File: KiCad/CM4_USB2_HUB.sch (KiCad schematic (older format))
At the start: 1 part

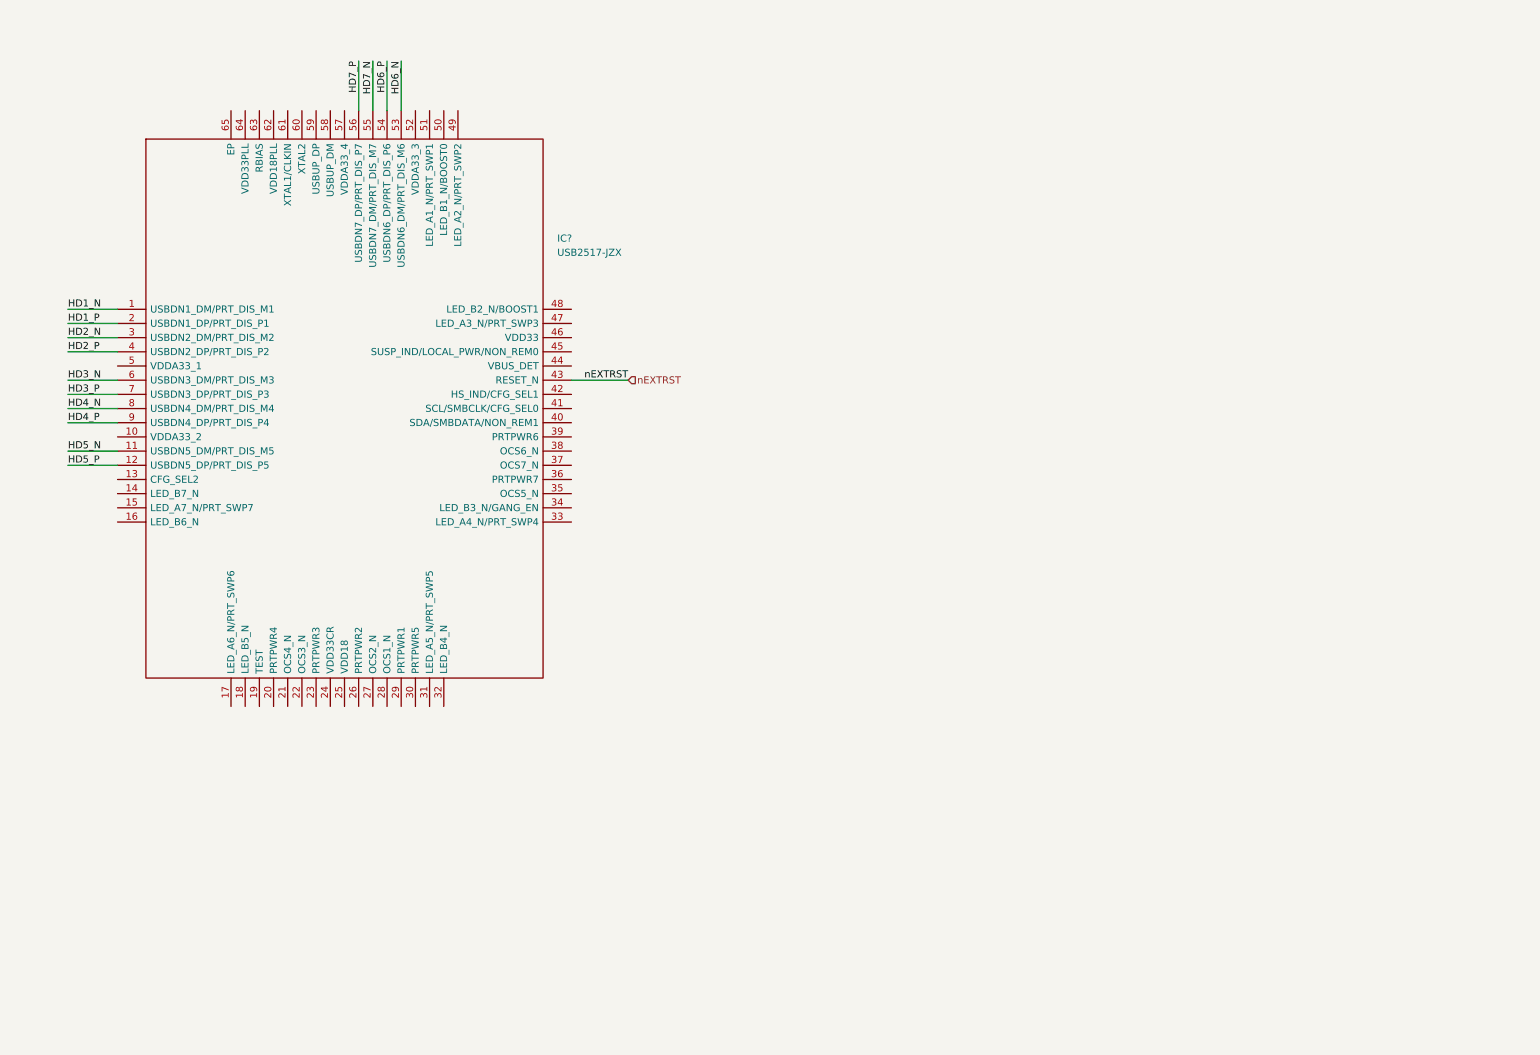
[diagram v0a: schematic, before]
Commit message: Lotsa changes
Added new footprints:
PCIe x1, TO-252 tab, SOT95, SOP50, SON50, Hirose FH-12-22S, 2.54mm 2x02 and 2x05 headers
Added new models:
Hirose FH-12-22S, FSUSB42MUX, MIC2019YM6-TR, TPS6206
Re-did ATX connector symbol wiring
Begun wiring PI7C PCI-e switch
Wired USB2517 hub
Begun adding MIC2019YM6 current limiters.
Added TODO lists to each page to help new contributors
Begun placing PCB footprints and descriptors
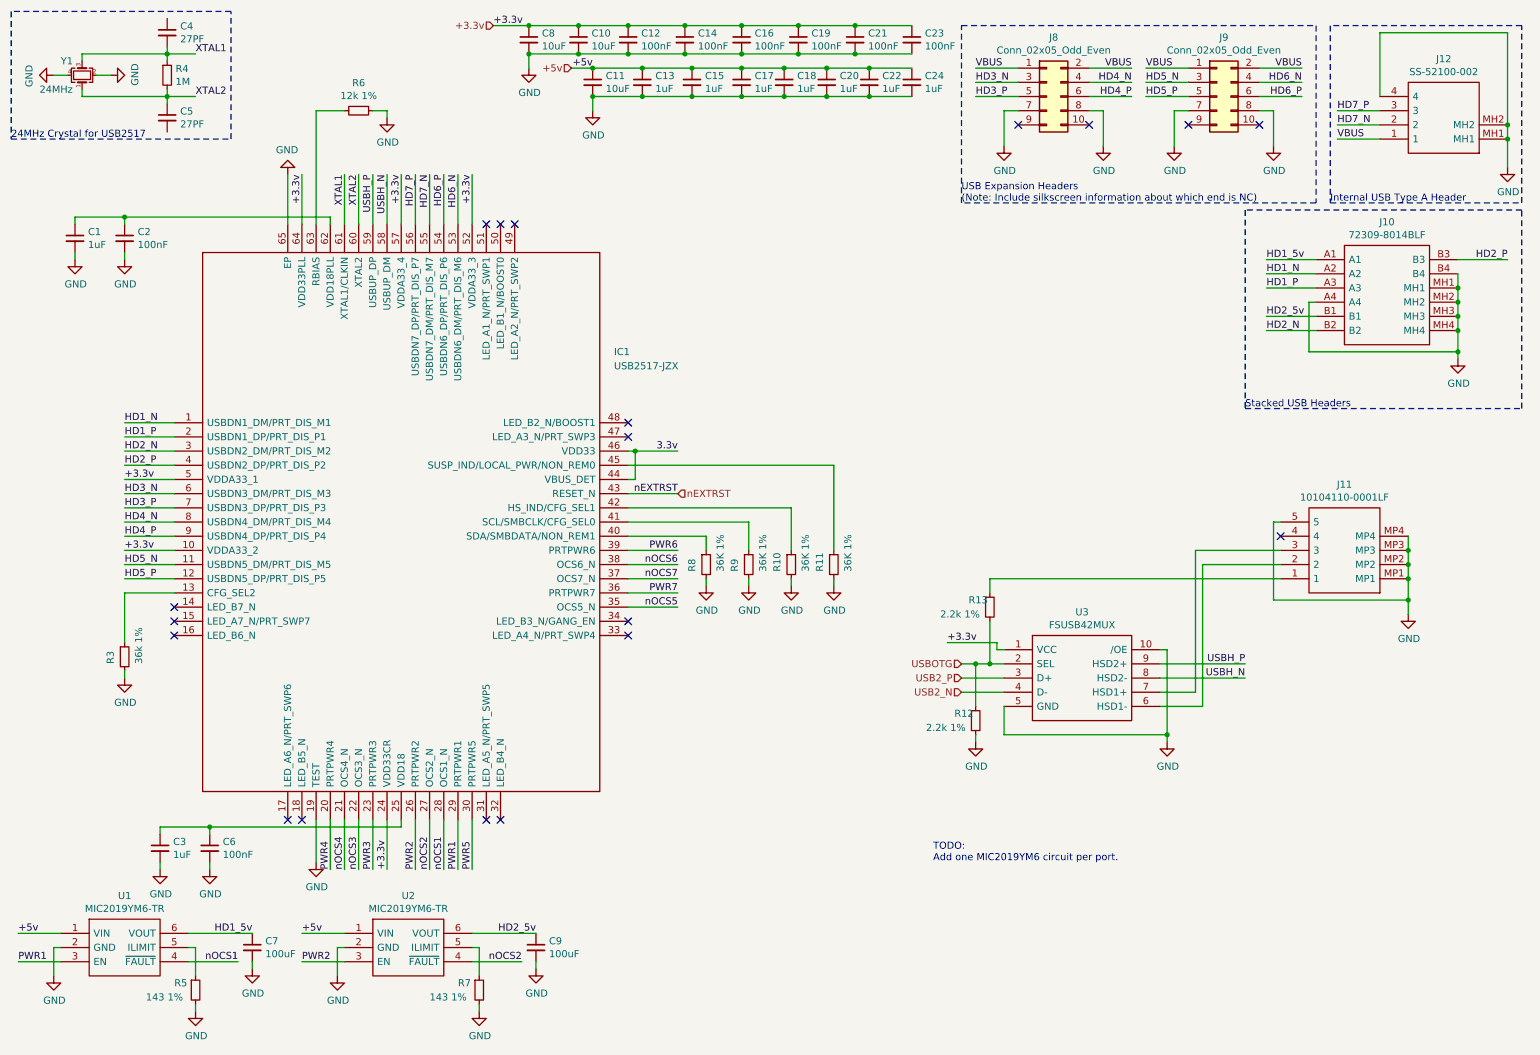
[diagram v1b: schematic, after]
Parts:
- added C1, C13, C15, C17, C18, C20, C22, C24, C3: 1uF, symbol Device:C_Small
- added C10, C11, C8: 10uF, symbol Device:C_Small
- added C12, C14, C16, C19, C2, C21, C23, C6: 100nF, symbol Device:C_Small
- added C4, C5: 27PF, symbol Device:C_Small
- added C7, C9: 100uF, symbol Device:C_Small
- added J10: 72309-8014BLF, 723098014BLF, symbol CM4_MATX:72309-8014BLF
- added J11: 10104110-0001LF, CM4_MATX:101041100001LF, symbol CM4_MATX:10104110-0001LF
- added J12: SS-52100-002, SS52100002, symbol CM4_MATX:SS-52100-002
- added J8, J9: Conn_02x05_Odd_Even, CM4_MATX:PinHeader_2x05_P2.54mm_Vertical, symbol Connector_Generic:Conn_02x05_Odd_Even
- added R10, R11, R8, R9: 36K 1%, symbol Device:R_Small
- added R12, R13: 2.2k 1%, symbol Device:R_Small
- added R3: 36k 1%, symbol Device:R_Small
- added R4: 1M, symbol Device:R_Small
- added R5, R7: 143 1%, symbol Device:R_Small
- added R6: 12k 1%, symbol Device:R_Small
- added U1, U2: MIC2019YM6-TR, SOT95P280X145-6N, symbol CM4_MATX:MIC2019YM6-TR
- added U3: FSUSB42MUX, SOP50P490X110-10N, symbol CM4_MATX:FSUSB42MUX
- added Y1: 24MHz, symbol Device:Crystal_GND24_Small
- gave numbers to parts that had none: 1
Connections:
- net HD1_N: now also J10.A2
- net HD1_P: now also J10.A3
- net HD2_N: now also J10.B2
- net HD2_P: now also J10.B3
- net HD3_N: now also J8.3 (Pin_3)
- net HD3_P: now also J8.5 (Pin_5)
- net HD4_N: now also J8.4 (Pin_4)
- net HD4_P: now also J8.6 (Pin_6)
- net HD5_N: now also J9.3 (Pin_3)
- net HD5_P: now also J9.5 (Pin_5)
- net HD6_N: now also J9.4 (Pin_4)
- net HD6_P: now also J9.6 (Pin_6)
- net HD7_N: now also J12.2
- net HD7_P: now also J12.3
- net +3.3v: now reaches IC1.10 (VDDA33_2)
- net +3.3v: now also IC1.24 (VDD33CR), IC1.5 (VDDA33_1), IC1.52 (VDDA33_3), IC1.57 (VDDA33_4), IC1.64 (VDD33PLL), C10.1, C12.1, C14.1, C16.1, C19.1, C21.1, C23.1, C8.1, U3.1 (VCC)
- net at IC1.13 (CFG_SEL2): now also R3.1
- net GND: now reaches IC1.19 (TEST)
- net GND: now also IC1.65 (EP), C1.2, C10.2, C11.2, C12.2, C13.2, C14.2, C15.2, C16.2, C17.2, C18.2, C19.2, C2.2, C20.2, C21.2, C22.2, C23.2, C24.2, C3.2, C6.2, C7.2, C8.2, C9.2, J10.A4, J10.B4, J10.MH1, J10.MH2, J10.MH3, J10.MH4, J11.5, J11.MP1, J11.MP2, J11.MP3, J11.MP4, J12.4, J12.MH1, J12.MH2, J8.7 (Pin_7), J8.8 (Pin_8), J9.7 (Pin_7), J9.8 (Pin_8), R10.2, R11.2, R12.2, R3.2, R5.2, R6.1, R7.2, R8.2, R9.2, U1.2 (GND), U2.2 (GND), U3.10 (/OE), U3.5 (GND), Y1.2, Y1.4
- net PWR4: now reaches IC1.20 (PRTPWR4)
- net nOCS4: now reaches IC1.21 (OCS4_N)
- net nOCS3: now reaches IC1.22 (OCS3_N)
- net PWR3: now reaches IC1.23 (PRTPWR3)
- net at IC1.25 (VDD18): now also C3.1, C6.1
- net PWR2: now reaches IC1.26 (PRTPWR2)
- net PWR2: now also U2.3 (EN)
- net nOCS2: now reaches IC1.27 (OCS2_N)
- net nOCS2: now also U2.4 (~FAULT)
- net nOCS1: now reaches IC1.28 (OCS1_N)
- net nOCS1: now also U1.4 (~FAULT)
- net PWR1: now reaches IC1.29 (PRTPWR1)
- net PWR1: now also U1.3 (EN)
- net PWR5: now reaches IC1.30 (PRTPWR5)
- net nOCS5: now reaches IC1.35 (OCS5_N)
- net PWR7: now reaches IC1.36 (PRTPWR7)
- net nOCS7: now reaches IC1.37 (OCS7_N)
- net nOCS6: now reaches IC1.38 (OCS6_N)
- net PWR6: now reaches IC1.39 (PRTPWR6)
- net at IC1.40 (SDA/SMBDATA/NON_REM1): now also R8.1
- net at IC1.41 (SCL/SMBCLK/CFG_SEL0): now also R9.1
- net at IC1.42 (HS_IND/CFG_SEL1): now also R10.1
- net 3.3v: now reaches IC1.44 (VBUS_DET)
- net 3.3v: now also IC1.46 (VDD33)
- net at IC1.45 (SUSP_IND/LOCAL_PWR/NON_REM0): now also R11.1
- net USBH_N: now reaches IC1.58 (USBUP_DM)
- net USBH_N: now also U3.8 (HSD2-)
- net USBH_P: now reaches IC1.59 (USBUP_DP)
- net USBH_P: now also U3.9 (HSD2+)
- net XTAL2: now reaches IC1.60 (XTAL2)
- net XTAL2: now also C5.1, R4.2, Y1.1
- net XTAL1: now reaches IC1.61 (XTAL1/CLKIN)
- net XTAL1: now also C4.2, R4.1, Y1.3
- net at IC1.62 (VDD18PLL): now also C1.1, C2.1
- net at IC1.63 (RBIAS): now also R6.2
- new net: J11.2, U3.6 (HSD1-)
- new net: J11.3, U3.7 (HSD1+)
- new net: J11.1, R13.1
- new net: R5.1, U1.5 (ILIMIT)
- new net: R7.1, U2.5 (ILIMIT)
- new net +5v: C11.1, C13.1, C15.1, C17.1, C18.1, C20.1, C22.1, C24.1, U1.1 (VIN), U2.1 (VIN)
- new net HD1_5v: C7.1, J10.A1, U1.6 (VOUT)
- new net HD2_5v: C9.1, J10.B1, U2.6 (VOUT)
- new net USB2_N: U3.4 (D-)
- new net USB2_P: U3.3 (D+)
- new net USBOTG: R12.1, R13.2, U3.2 (SEL)
- new net VBUS: J12.1, J8.1 (Pin_1), J8.2 (Pin_2), J9.1 (Pin_1), J9.2 (Pin_2)
- no-connect marks 0 -> 19
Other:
- note added: "24MHz Crystal for USB2517"
- note added: "Internal USB Type A Header"
- note added: "Stacked USB Headers"
- note added: "TODO:\nAdd one MIC2019YM6 circuit per port."
- note added: "USB Expansion Headers\n(Note: Include silkscreen information about which end is NC)"
- moved on the sheet: IC1

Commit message: Many, many changes...
Added a bunch of new footprints and a couple of new symbols.
Added the other side of the CM4 connector and wired its features.
Added some more detailed models for a fair few components.
Added a new schematic to handle power for USB ports.
Updated the PCB with the new components and moved some around to populate the rear IO panel.
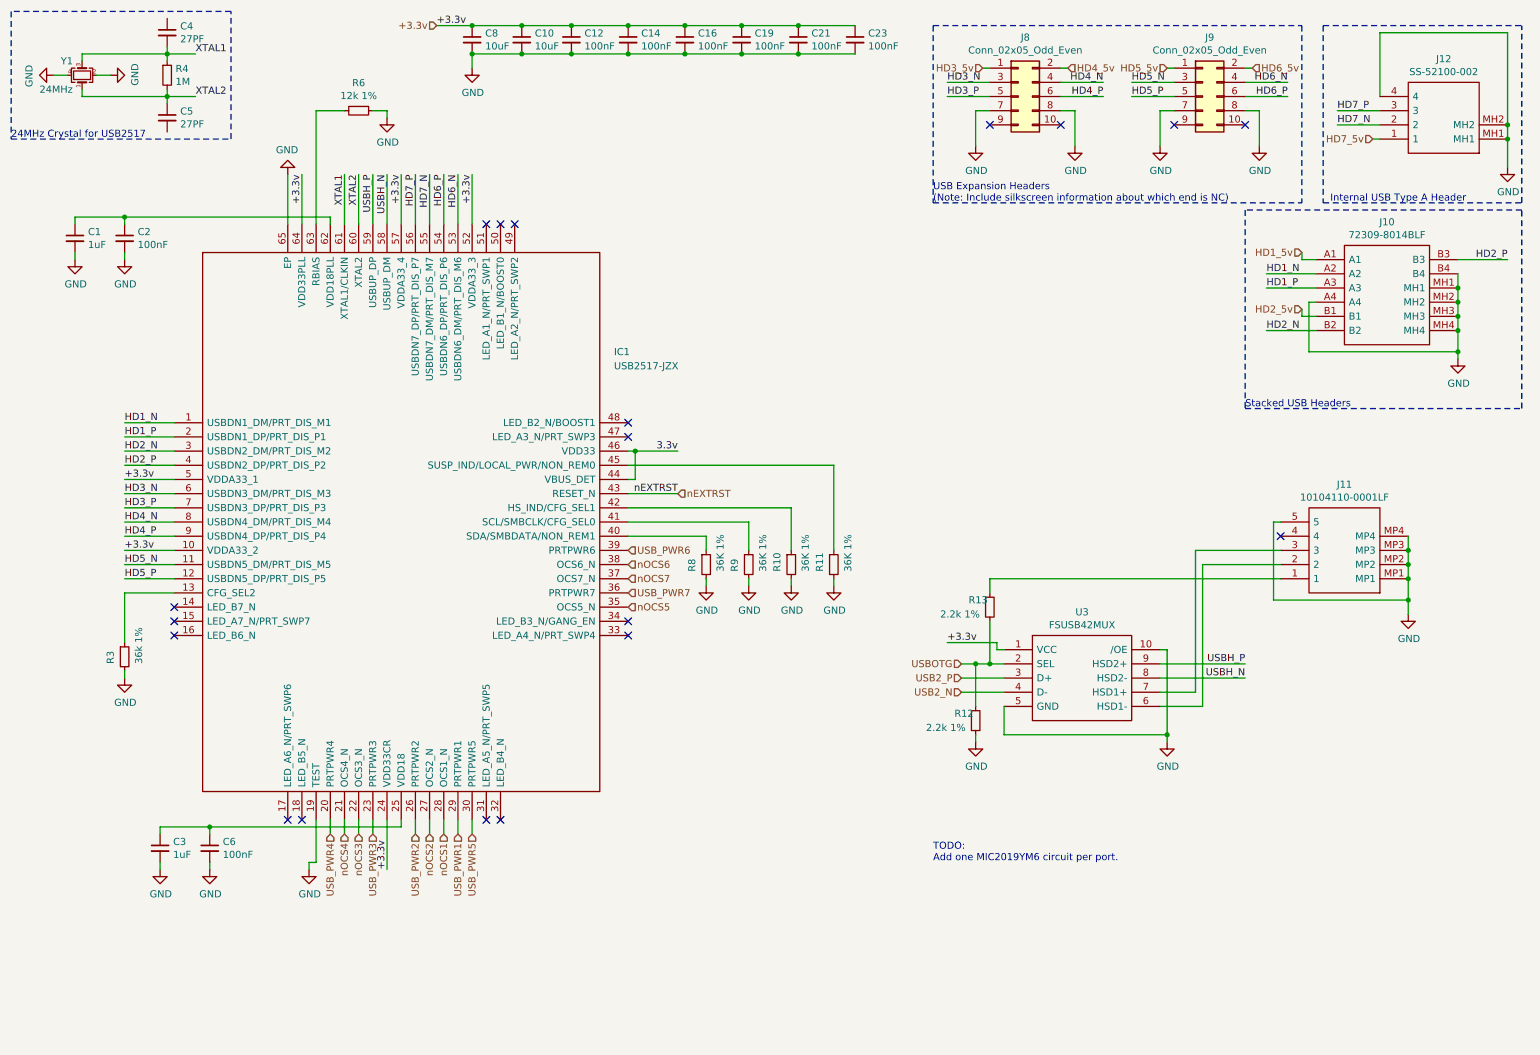
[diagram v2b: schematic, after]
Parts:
- removed C11: 10uF, symbol Device:C_Small
- removed C13, C15, C17, C18, C20, C22, C24: 1uF, symbol Device:C_Small
- removed C7, C9: 100uF, symbol Device:C_Small
- removed R5, R7: 143 1%, symbol Device:R_Small
- removed U1, U2: MIC2019YM6-TR, SOT95P280X145-6N, symbol CM4_MATX:MIC2019YM6-TR
- IC1: footprint QFN50P900X900X100-65N-D -> CM4_MATX:QFN50P900X900X100-65N-D
- J10: footprint 723098014BLF -> CM4_MATX:723098014BLF
- J12: footprint SS52100002 -> CM4_MATX:SS52100002
- U3: footprint SOP50P490X110-10N -> CM4_MATX:SOP50P490X110-10N
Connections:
- net PWR1 renamed USB_PWR1
- net PWR2 renamed USB_PWR2
- net PWR3 renamed USB_PWR3
- net PWR4 renamed USB_PWR4
- net PWR5 renamed USB_PWR5
- net PWR6 renamed USB_PWR6
- net PWR7 renamed USB_PWR7
- removed net VBUS: J12.1, J8.1 (Pin_1), J8.2 (Pin_2), J9.1 (Pin_1), J9.2 (Pin_2)
- new net HD3_5v: J8.1 (Pin_1)
- new net HD4_5v: J8.2 (Pin_2)
- new net HD5_5v: J9.1 (Pin_1)
- new net HD6_5v: J9.2 (Pin_2)
- new net HD7_5v: J12.1
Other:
- moved on the sheet: C10, C12, C14, C16, C19, C21, C23, C8, J8, J9

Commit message: Small changes to PCIe, USB Schematics and board layout, legend for GPIO pins.
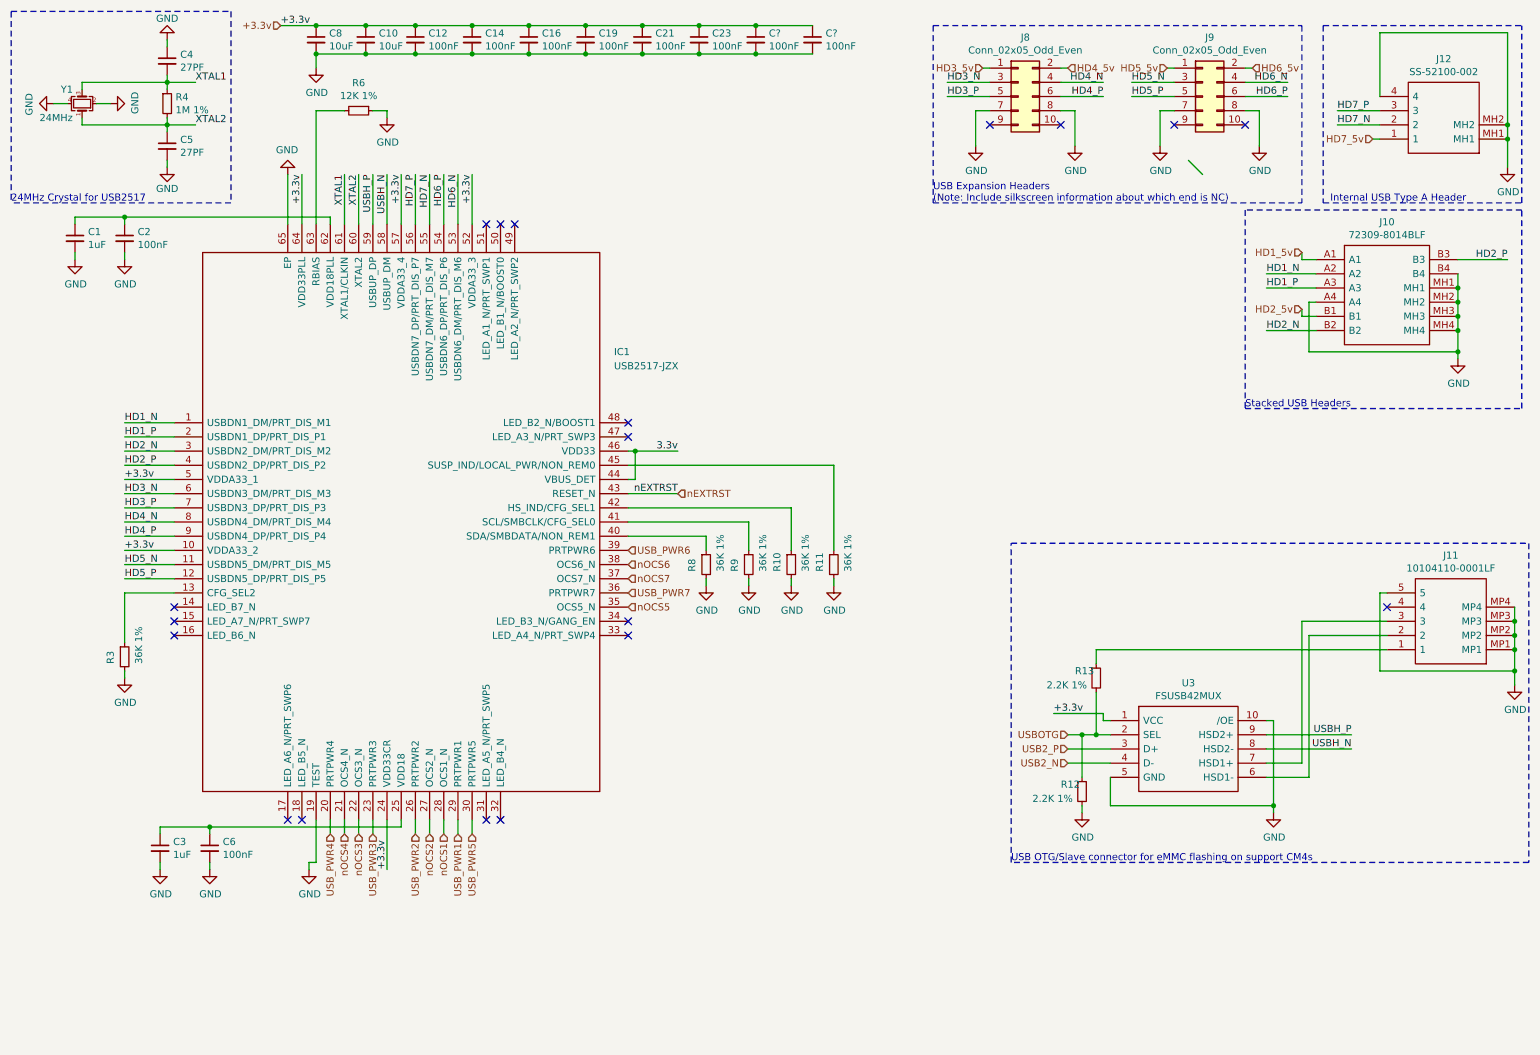
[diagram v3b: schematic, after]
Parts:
- added C? (x2): 100nF, symbol Device:C_Small
- R12, R13: value 2.2k 1% -> 2.2K 1%
- R3: value 36k 1% -> 36K 1%
- R4: value 1M -> 1M 1%
- R6: value 12k 1% -> 12K 1%
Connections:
- net +3.3v: now also C?.1, C?.1
- net GND: now also C4.1, C5.2, C?.2, C?.2
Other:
- note added: "USB OTG/Slave connector for eMMC flashing on support CM4s"
- note removed: "TODO:\nAdd one MIC2019YM6 circuit per port."
- moved on the sheet: C10, C12, C14, C16, C19, C21, C23, C4, C5, C8, J11, R12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

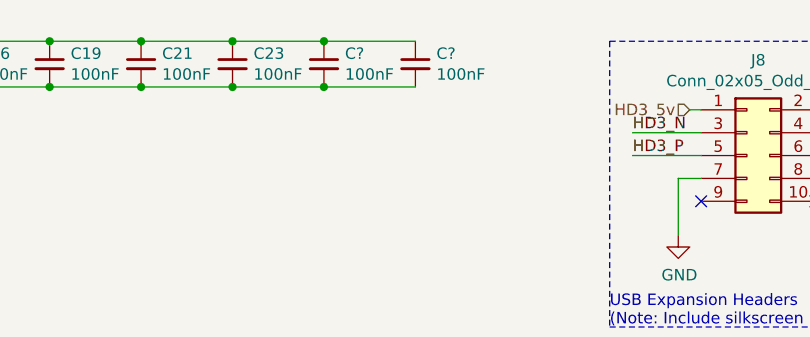
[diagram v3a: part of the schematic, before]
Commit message: Added License text, fixes #30, updated PCB to include copyright notice.
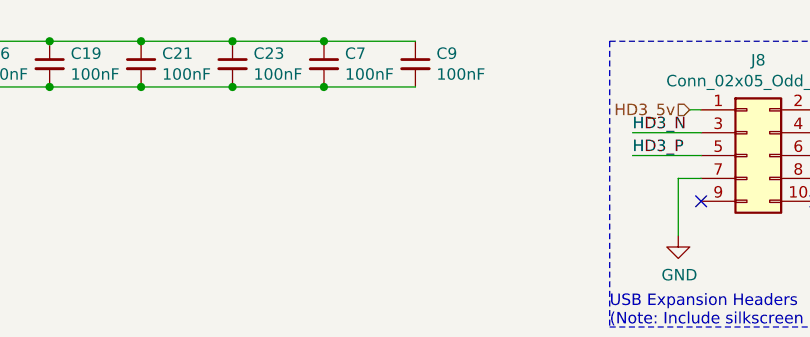
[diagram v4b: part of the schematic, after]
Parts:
- gave numbers to parts that had none: 2
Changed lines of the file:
@@
 Sheet 4 10
 Title "CM4_MATX: USB Hub and Ports"
-Date "2020-11-27"
+Date "2020-12-14"
 Rev "0.1"
-Comp "CM4_MATX Contributors"
+Comp "Copyright Oliver Møller/@TheGuyDanish 2020, CERN OHL-P v2"
 Comment1 "https://github.com/theguydanish/CM4_MATX"
 Comment2 ""
@@
 	9600 2250 9700 2250
 $Comp
-L Device:C_Small C?
+L Device:C_Small C7
 U 1 1 5FCA3246
 P 5750 700
-F 0 "C?" H 5842 746 50  0000 L CNN
+F 0 "C7" H 5842 746 50  0000 L CNN
 F 1 "100nF" H 5842 655 50  0000 L CNN
 F 2 "" H 5750 700 50  0001 C CNN
@@
 Connection ~ 5350 800
 $Comp
-L Device:C_Small C?
+L Device:C_Small C9
 U 1 1 5FCC6E0E
 P 6150 700
-F 0 "C?" H 6242 746 50  0000 L CNN
+F 0 "C9" H 6242 746 50  0000 L CNN
 F 1 "100nF" H 6242 655 50  0000 L CNN
 F 2 "" H 6150 700 50  0001 C CNN
@@
 Connection ~ 5750 800
 $Comp
-L power:GND #PWR?
+L power:GND #PWR0133
 U 1 1 5FCE87B8
 P 1600 1600
-F 0 "#PWR?" H 1600 1350 50  0001 C CNN
+F 0 "#PWR0133" H 1600 1350 50  0001 C CNN
 F 1 "GND" H 1600 1450 50  0000 C CNN
 F 2 "" H 1600 1600 50  0001 C CNN
@@
 	1600 1550 1600 1600
 $Comp
-L power:GND #PWR?
+L power:GND #PWR0134
 U 1 1 5FCF3652
 P 1600 700
-F 0 "#PWR?" H 1600 450 50  0001 C CNN
+F 0 "#PWR0134" H 1600 450 50  0001 C CNN
 F 1 "GND" H 1600 550 50  0000 C CNN
 F 2 "" H 1600 700 50  0001 C CNN
